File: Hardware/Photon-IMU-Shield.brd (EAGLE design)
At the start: 40.6 x 35.6 mm, 26 parts, among them U1 LSM9DS1

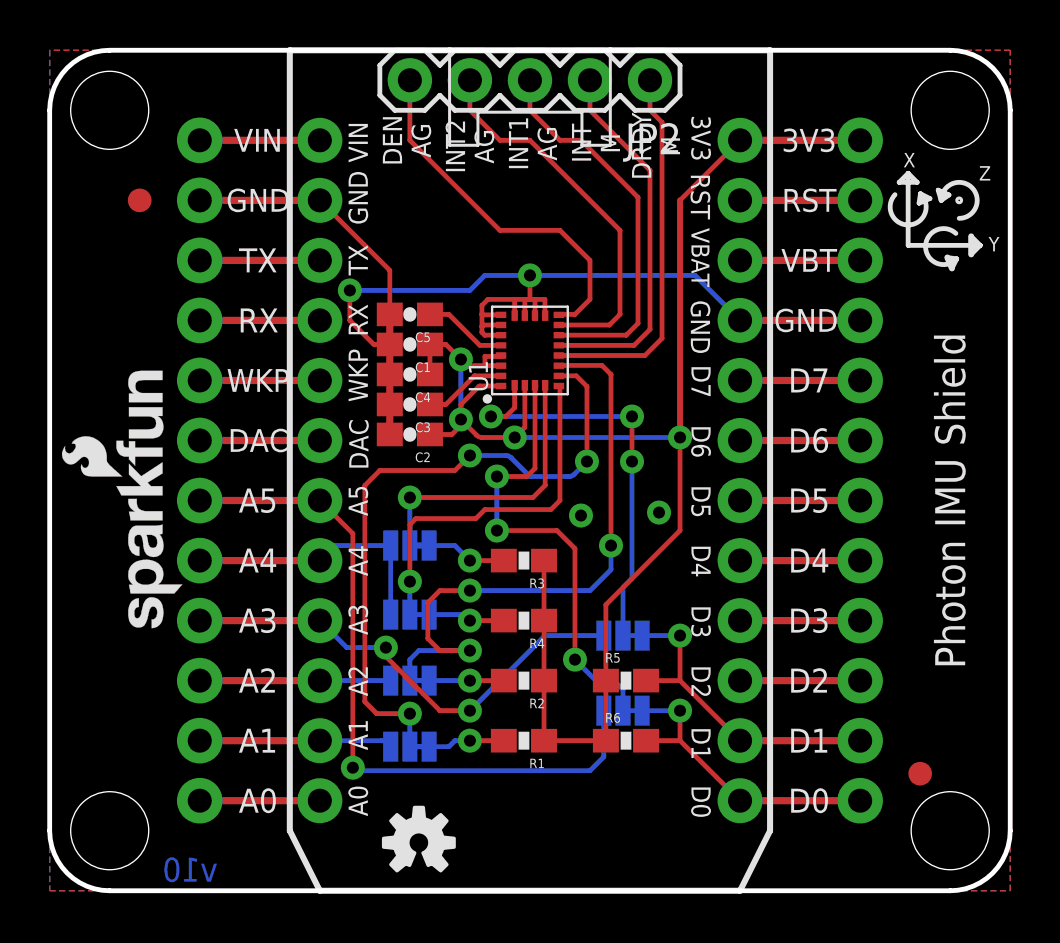
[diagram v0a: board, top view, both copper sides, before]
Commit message: Small silkscreen changes.
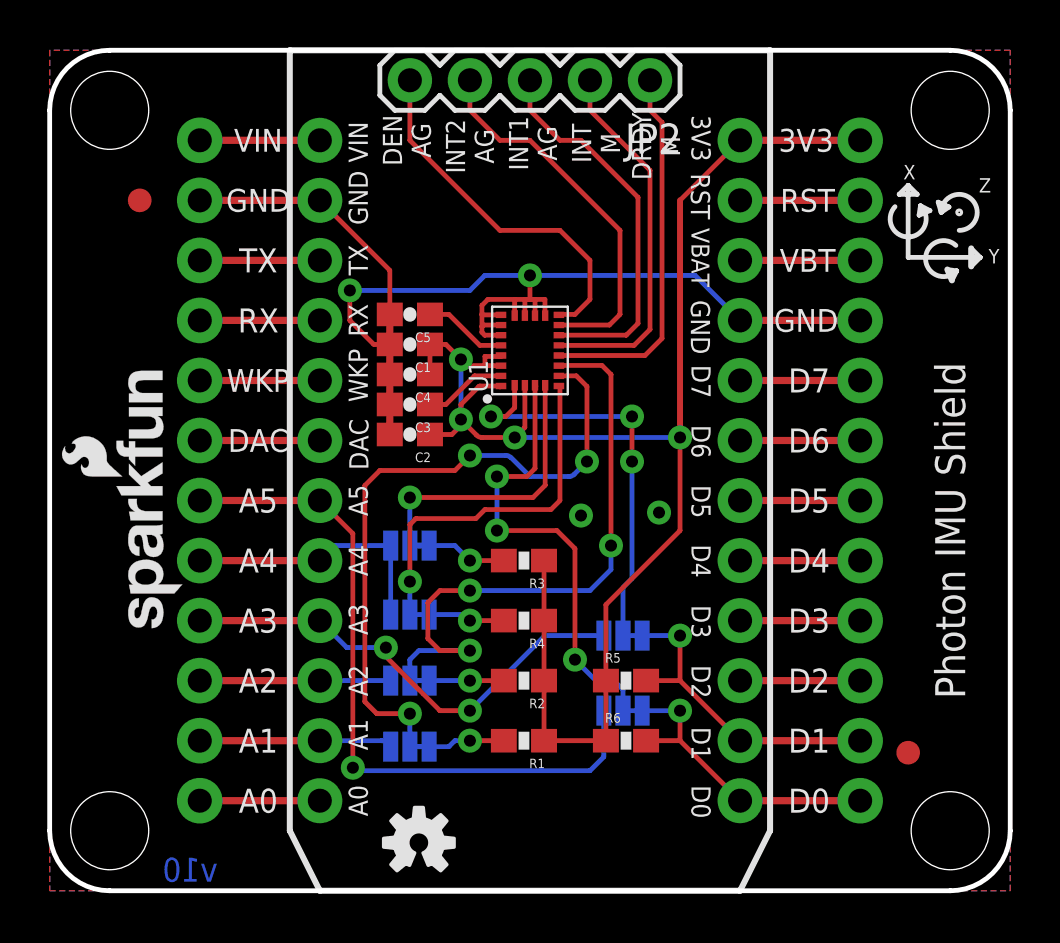
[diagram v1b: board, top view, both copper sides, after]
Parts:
- moved FID2 1.02 mm to (33.8, 5.84)
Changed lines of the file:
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@@
 <board>
 <plain>
-<text x="35.56" y="16.51" size="1.27" layer="21" font="vector" ratio="15" rot="R90" align="center">Photon IMU Shield</text>
+<text x="35.56" y="15.24" size="1.27" layer="21" font="vector" ratio="15" rot="R90" align="center">Photon IMU Shield</text>
 <text x="17.526" y="14.732" size="0.8128" layer="22" font="vector" ratio="15" rot="MR270" align="bottom-center">SDO
 A/G</text>
@@
 <text x="24.5872" y="30.353" size="0.8128" layer="21" font="vector" ratio="12" rot="SR270">RST</text>
 <text x="24.6126" y="32.8168" size="0.8128" layer="21" font="vector" ratio="12" rot="SR270">3V3</text>
-<text x="33.8328" y="30.607" size="0.6096" layer="21" font="vector" ratio="12" align="bottom-center">X</text>
-<text x="37.4142" y="27.051" size="0.6096" layer="21" font="vector" ratio="12" align="bottom-center">Y</text>
-<text x="37.0332" y="30.0482" size="0.6096" layer="21" font="vector" ratio="12" align="bottom-center">Z</text>
-<circle x="35.941" y="29.21" radius="0.0635" width="0.2032" layer="21"/>
-<wire x1="35.179" y1="29.21" x2="35.941" y2="28.448" width="0.2032" layer="21" curve="-270"/>
-<wire x1="35.179" y1="29.21" x2="35.5092" y2="29.4386" width="0.2032" layer="21"/>
-<wire x1="35.5092" y1="29.4386" x2="35.052" y2="29.6418" width="0.2032" layer="21"/>
-<wire x1="35.052" y1="29.6418" x2="35.179" y2="29.21" width="0.2032" layer="21"/>
-<wire x1="35.306" y1="29.337" x2="35.179" y2="29.337" width="0.127" layer="21"/>
-<wire x1="35.2806" y1="29.4386" x2="35.2044" y2="29.5402" width="0.254" layer="21"/>
-<wire x1="35.836984375" y1="26.733546875" x2="35.80125625" y2="27.810584375" width="0.2032" layer="21" curve="-270"/>
-<wire x1="35.836984375" y1="26.733546875" x2="35.439690625" y2="26.79225" width="0.2032" layer="21"/>
-<wire x1="35.439690625" y1="26.79225" x2="35.634678125" y2="26.3314875" width="0.254" layer="21"/>
-<wire x1="35.634678125" y1="26.3314875" x2="35.836984375" y2="26.733546875" width="0.2032" layer="21"/>
-<wire x1="33.782" y1="27.305" x2="36.83" y2="27.305" width="0.2032" layer="21"/>
-<wire x1="33.782" y1="27.305" x2="33.782" y2="30.353" width="0.2032" layer="21"/>
-<wire x1="36.83" y1="27.305" x2="36.449" y2="26.924" width="0.2032" layer="21"/>
-<wire x1="36.449" y1="26.924" x2="36.449" y2="27.686" width="0.254" layer="21"/>
-<wire x1="36.449" y1="27.686" x2="36.83" y2="27.305" width="0.2032" layer="21"/>
-<wire x1="33.401" y1="29.972" x2="33.782" y2="30.353" width="0.2032" layer="21"/>
-<wire x1="34.163" y1="29.972" x2="33.401" y2="29.972" width="0.2032" layer="21"/>
-<wire x1="33.782" y1="30.353" x2="34.163" y2="29.972" width="0.2032" layer="21"/>
-<wire x1="34.302653125" y1="29.486984375" x2="33.225615625" y2="29.45125625" width="0.2032" layer="21" curve="-270"/>
-<wire x1="34.302653125" y1="29.486984375" x2="34.24395" y2="29.089690625" width="0.2032" layer="21"/>
-<wire x1="34.24395" y1="29.089690625" x2="34.7047125" y2="29.284678125" width="0.2032" layer="21"/>
-<wire x1="34.7047125" y1="29.284678125" x2="34.302653125" y2="29.486984375" width="0.2032" layer="21"/>
+<text x="33.8328" y="30.099" size="0.6096" layer="21" font="vector" ratio="12" align="bottom-center">X</text>
+<text x="37.4142" y="26.543" size="0.6096" layer="21" font="vector" ratio="12" align="bottom-center">Y</text>
+<text x="37.0332" y="29.5402" size="0.6096" layer="21" font="vector" ratio="12" align="bottom-center">Z</text>
+<circle x="35.941" y="28.702" radius="0.0635" width="0.2032" layer="21"/>
+<wire x1="35.179" y1="28.702" x2="35.941" y2="27.94" width="0.2032" layer="21" curve="-270"/>
+<wire x1="35.179" y1="28.702" x2="35.5092" y2="28.9306" width="0.2032" layer="21"/>
+<wire x1="35.5092" y1="28.9306" x2="35.052" y2="29.1338" width="0.2032" layer="21"/>
+<wire x1="35.052" y1="29.1338" x2="35.179" y2="28.702" width="0.2032" layer="21"/>
+<wire x1="35.306" y1="28.829" x2="35.179" y2="28.829" width="0.127" layer="21"/>
+<wire x1="35.2806" y1="28.9306" x2="35.2044" y2="29.0322" width="0.254" layer="21"/>
+<wire x1="35.836984375" y1="26.225546875" x2="35.80125625" y2="27.302584375" width="0.2032" layer="21" curve="-270"/>
+<wire x1="35.836984375" y1="26.225546875" x2="35.439690625" y2="26.28425" width="0.2032" layer="21"/>
+<wire x1="35.439690625" y1="26.28425" x2="35.634678125" y2="25.8234875" width="0.254" layer="21"/>
+<wire x1="35.634678125" y1="25.8234875" x2="35.836984375" y2="26.225546875" width="0.2032" layer="21"/>
+<wire x1="33.782" y1="26.797" x2="36.83" y2="26.797" width="0.2032" layer="21"/>
+<wire x1="33.782" y1="26.797" x2="33.782" y2="29.845" width="0.2032" layer="21"/>
+<wire x1="36.83" y1="26.797" x2="36.449" y2="26.416" width="0.2032" layer="21"/>
+<wire x1="36.449" y1="26.416" x2="36.449" y2="27.178" width="0.254" layer="21"/>
+<wire x1="36.449" y1="27.178" x2="36.83" y2="26.797" width="0.2032" layer="21"/>
+<wire x1="33.401" y1="29.464" x2="33.782" y2="29.845" width="0.2032" layer="21"/>
+<wire x1="34.163" y1="29.464" x2="33.401" y2="29.464" width="0.2032" layer="21"/>
+<wire x1="33.782" y1="29.845" x2="34.163" y2="29.464" width="0.2032" layer="21"/>
+<wire x1="34.302653125" y1="28.978984375" x2="33.225615625" y2="28.94325625" width="0.2032" layer="21" curve="-270"/>
+<wire x1="34.302653125" y1="28.978984375" x2="34.24395" y2="28.581690625" width="0.2032" layer="21"/>
+<wire x1="34.24395" y1="28.581690625" x2="34.7047125" y2="28.776678125" width="0.2032" layer="21"/>
+<wire x1="34.7047125" y1="28.776678125" x2="34.302653125" y2="28.978984375" width="0.2032" layer="21"/>
 <wire x1="0" y1="35.56" x2="35.56" y2="35.56" width="0.2032" layer="20"/>
 <wire x1="35.56" y1="0" x2="0" y2="0" width="0.2032" layer="20"/>
@@
 <dimension x1="2.54" y1="2.54" x2="0.889" y2="2.54" x3="1.7145" y3="-2.54" textsize="0.8128" textratio="15" layer="47" dtype="diameter" unit="inch" precision="3"/>
 <text x="0" y="-11.43" size="0.8128" layer="47" font="vector" ratio="15">Units in Inches</text>
-<text x="35.56" y="16.51" size="1.27" layer="22" font="vector" ratio="15" rot="MR270" align="center">Photon IMU Shield</text>
+<text x="35.56" y="15.24" size="1.27" layer="22" font="vector" ratio="15" rot="MR270" align="center">Photon IMU Shield</text>
 </plain>
 <attributes>
@@
 <element name="U$5" library="SparkFun-Aesthetics" package="SFE_LOGO_NAME_FLAME_.1" value="" x="17.653" y="18.542" rot="MR90"/>
 <element name="FID1" library="SparkFun-Aesthetics" package="FIDUCIAL-1X2" value="FIDUCIAL1X2" x="1.27" y="29.21"/>
-<element name="FID2" library="SparkFun-Aesthetics" package="FIDUCIAL-1X2" value="FIDUCIAL1X2" x="34.29" y="4.953"/>
+<element name="FID2" library="SparkFun-Aesthetics" package="FIDUCIAL-1X2" value="FIDUCIAL1X2" x="33.782" y="5.842"/>
 <element name="LOGO2" library="SparkFun-Aesthetics" package="OSHW-LOGO-S" value="OSHW-LOGOS" x="13.081" y="2.032"/>
 <element name="JP2" library="SparkFun-Connectors" package="1X05" value="" x="22.86" y="34.29" rot="R180"/>
